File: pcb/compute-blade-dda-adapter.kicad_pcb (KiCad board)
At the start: 2 copper layers, 49 x 16 mm, 2 parts, among them J1 HLE-105-02-L-DV-PE-BE, J2 MTLW-106-06-G-D-035 REVERSE

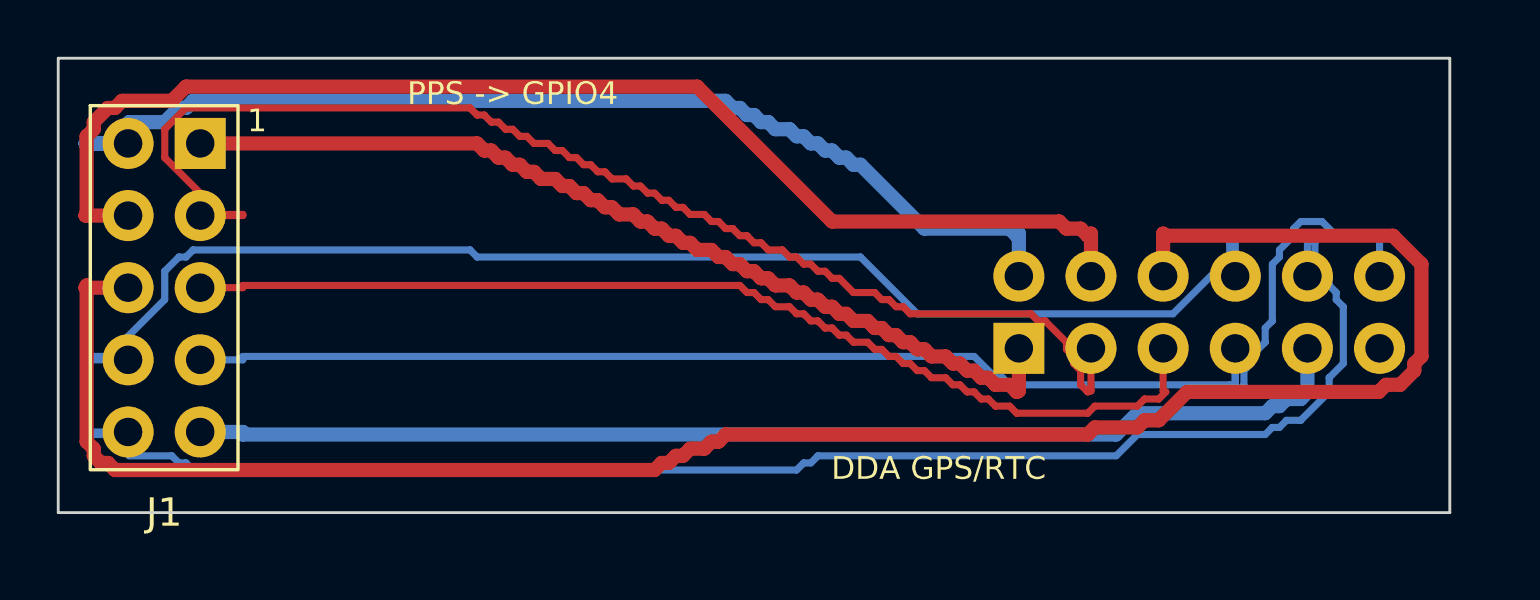
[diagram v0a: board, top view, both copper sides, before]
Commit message: Respect square pin-one pad clearances
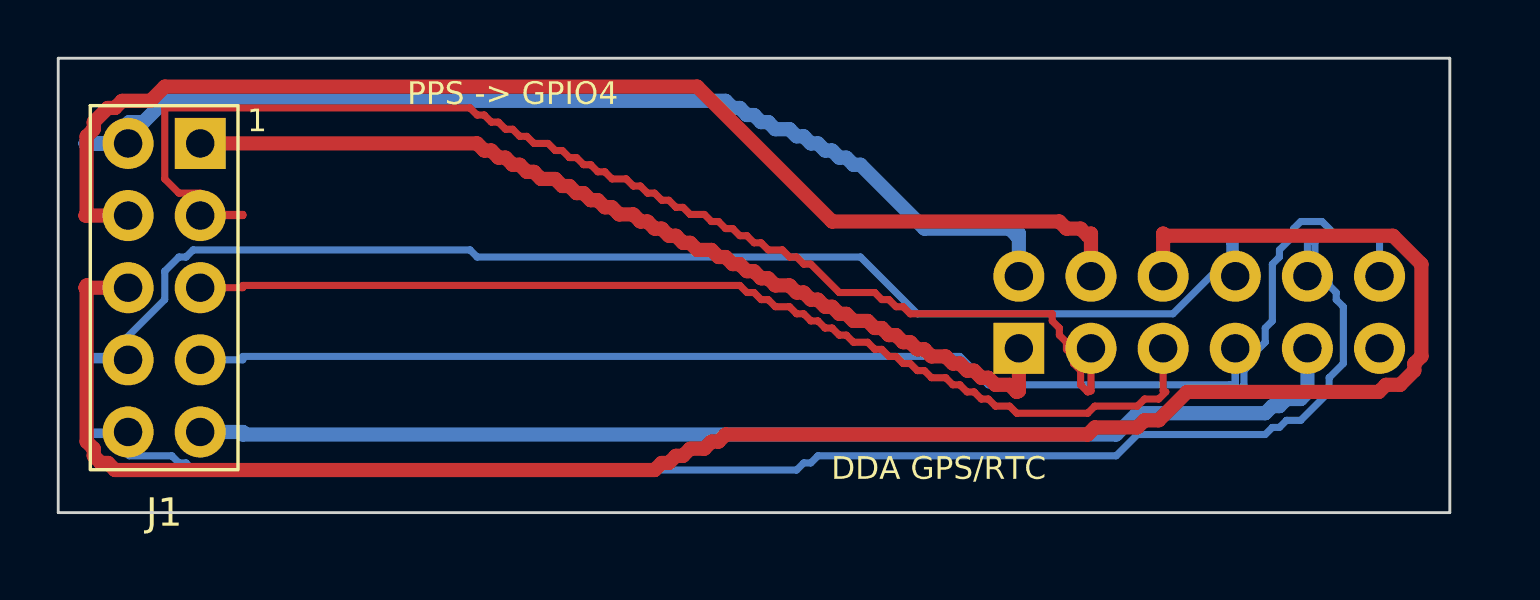
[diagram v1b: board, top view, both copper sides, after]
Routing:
- net SDA_GPIO2: track 45.3 -> 46.4 mm
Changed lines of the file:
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@@
   (segment (start 95.96 60.16) (end 96.75 60.16) (width 0.5) (layer "B.Cu") (net 2))
   (segment (start 96.75 60.16) (end 97.5 59.41) (width 0.5) (layer "B.Cu") (net 2))
-  (segment (start 97.5 59.41) (end 98.75 59.41) (width 0.5) (layer "B.Cu") (net 2))
-  (segment (start 98.75 59.41) (end 99.25 58.91) (width 0.5) (layer "B.Cu") (net 2))
-  (segment (start 99.25 58.91) (end 99.5 58.91) (width 0.5) (layer "B.Cu") (net 2))
-  (segment (start 99.5 58.91) (end 99.75 58.66) (width 0.5) (layer "B.Cu") (net 2))
-  (segment (start 99.75 58.66) (end 118.5 58.66) (width 0.5) (layer "B.Cu") (net 2))
+  (segment (start 97.5 59.41) (end 98 59.41) (width 0.5) (layer "B.Cu") (net 2))
+  (segment (start 98 59.41) (end 98.75 58.66) (width 0.5) (layer "B.Cu") (net 2))
+  (segment (start 98.75 58.66) (end 118.5 58.66) (width 0.5) (layer "B.Cu") (net 2))
   (segment (start 118.5 58.66) (end 118.75 58.91) (width 0.5) (layer "B.Cu") (net 2))
   (segment (start 118.75 58.91) (end 119 58.91) (width 0.5) (layer "B.Cu") (net 2))
@@
   (segment (start 101.5 62.7) (end 101.5 62.66) (width 0.25) (layer "F.Cu") (net 3))
   (segment (start 101.5 62.66) (end 100.75 62.66) (width 0.25) (layer "F.Cu") (net 3))
-  (segment (start 100.75 62.66) (end 98.75 60.66) (width 0.25) (layer "F.Cu") (net 3))
-  (segment (start 98.75 60.66) (end 98.75 59.66) (width 0.25) (layer "F.Cu") (net 3))
-  (segment (start 98.75 59.66) (end 99.5 58.91) (width 0.25) (layer "F.Cu") (net 3))
-  (segment (start 99.5 58.91) (end 109.5 58.91) (width 0.25) (layer "F.Cu") (net 3))
+  (segment (start 100.75 62.66) (end 100 61.91) (width 0.25) (layer "F.Cu") (net 3))
+  (segment (start 100 61.91) (end 99.25 61.91) (width 0.25) (layer "F.Cu") (net 3))
+  (segment (start 99.25 61.91) (end 98.75 61.41) (width 0.25) (layer "F.Cu") (net 3))
+  (segment (start 98.75 61.41) (end 98.75 58.91) (width 0.25) (layer "F.Cu") (net 3))
+  (segment (start 98.75 58.91) (end 109.5 58.91) (width 0.25) (layer "F.Cu") (net 3))
   (segment (start 109.5 58.91) (end 109.75 59.16) (width 0.25) (layer "F.Cu") (net 3))
   (segment (start 109.75 59.16) (end 110 59.16) (width 0.25) (layer "F.Cu") (net 3))
@@
   (segment (start 121 64.16) (end 121.25 64.41) (width 0.25) (layer "F.Cu") (net 3))
   (segment (start 121.25 64.41) (end 121.5 64.41) (width 0.25) (layer "F.Cu") (net 3))
-  (segment (start 121.5 64.41) (end 121.75 64.66) (width 0.25) (layer "F.Cu") (net 3))
-  (segment (start 121.75 64.66) (end 122 64.66) (width 0.25) (layer "F.Cu") (net 3))
-  (segment (start 122 64.66) (end 122.25 64.91) (width 0.25) (layer "F.Cu") (net 3))
-  (segment (start 122.25 64.91) (end 122.5 64.91) (width 0.25) (layer "F.Cu") (net 3))
-  (segment (start 122.5 64.91) (end 123 65.41) (width 0.25) (layer "F.Cu") (net 3))
-  (segment (start 123 65.41) (end 123.75 65.41) (width 0.25) (layer "F.Cu") (net 3))
+  (segment (start 121.5 64.41) (end 122.5 65.41) (width 0.25) (layer "F.Cu") (net 3))
+  (segment (start 122.5 65.41) (end 123.75 65.41) (width 0.25) (layer "F.Cu") (net 3))
   (segment (start 123.75 65.41) (end 124 65.66) (width 0.25) (layer "F.Cu") (net 3))
   (segment (start 124 65.66) (end 124.25 65.66) (width 0.25) (layer "F.Cu") (net 3))
@@
   (segment (start 124.5 65.91) (end 124.75 65.91) (width 0.25) (layer "F.Cu") (net 3))
   (segment (start 124.75 65.91) (end 125 66.16) (width 0.25) (layer "F.Cu") (net 3))
-  (segment (start 125 66.16) (end 129.25 66.16) (width 0.25) (layer "F.Cu") (net 3))
-  (segment (start 129.25 66.16) (end 129.5 66.41) (width 0.25) (layer "F.Cu") (net 3))
-  (segment (start 129.5 66.41) (end 129.75 66.41) (width 0.25) (layer "F.Cu") (net 3))
-  (segment (start 129.75 66.41) (end 130.5 67.16) (width 0.25) (layer "F.Cu") (net 3))
+  (segment (start 125 66.16) (end 130 66.16) (width 0.25) (layer "F.Cu") (net 3))
+  (segment (start 130 66.16) (end 130 66.41) (width 0.25) (layer "F.Cu") (net 3))
+  (segment (start 130 66.41) (end 130.25 66.66) (width 0.25) (layer "F.Cu") (net 3))
+  (segment (start 130.25 66.66) (end 130.25 66.91) (width 0.25) (layer "F.Cu") (net 3))
+  (segment (start 130.25 66.91) (end 130.5 67.16) (width 0.25) (layer "F.Cu") (net 3))
   (segment (start 130.5 67.16) (end 130.5 67.41) (width 0.25) (layer "F.Cu") (net 3))
   (segment (start 130.5 67.41) (end 130.75 67.66) (width 0.25) (layer "F.Cu") (net 3))
@@
   (segment (start 96.75 58.91) (end 97 58.91) (width 0.5) (layer "F.Cu") (net 4))
   (segment (start 97 58.91) (end 97.25 58.66) (width 0.5) (layer "F.Cu") (net 4))
-  (segment (start 97.25 58.66) (end 99 58.66) (width 0.5) (layer "F.Cu") (net 4))
-  (segment (start 99 58.66) (end 99.5 58.16) (width 0.5) (layer "F.Cu") (net 4))
-  (segment (start 99.5 58.16) (end 117.5 58.16) (width 0.5) (layer "F.Cu") (net 4))
+  (segment (start 97.25 58.66) (end 98.25 58.66) (width 0.5) (layer "F.Cu") (net 4))
+  (segment (start 98.25 58.66) (end 98.75 58.16) (width 0.5) (layer "F.Cu") (net 4))
+  (segment (start 98.75 58.16) (end 117.5 58.16) (width 0.5) (layer "F.Cu") (net 4))
   (segment (start 117.5 58.16) (end 122.25 62.91) (width 0.5) (layer "F.Cu") (net 4))
   (segment (start 122.25 62.91) (end 130.25 62.91) (width 0.5) (layer "F.Cu") (net 4))
@@
   (segment (start 100 67.78) (end 101.5 67.78) (width 0.25) (layer "B.Cu") (net 7))
   (segment (start 101.5 67.78) (end 101.5 67.66) (width 0.25) (layer "B.Cu") (net 7))
-  (segment (start 101.5 67.66) (end 127.25 67.66) (width 0.25) (layer "B.Cu") (net 7))
-  (segment (start 127.25 67.66) (end 128 68.41) (width 0.25) (layer "B.Cu") (net 7))
-  (segment (start 128 68.41) (end 128.25 68.41) (width 0.25) (layer "B.Cu") (net 7))
-  (segment (start 128.25 68.41) (end 128.5 68.66) (width 0.25) (layer "B.Cu") (net 7))
-  (segment (start 128.5 68.66) (end 136.25 68.66) (width 0.25) (layer "B.Cu") (net 7))
+  (segment (start 101.5 67.66) (end 126.75 67.66) (width 0.25) (layer "B.Cu") (net 7))
+  (segment (start 126.75 67.66) (end 127.75 68.66) (width 0.25) (layer "B.Cu") (net 7))
+  (segment (start 127.75 68.66) (end 136.25 68.66) (width 0.25) (layer "B.Cu") (net 7))
   (segment (start 136.25 68.66) (end 136.5 68.91) (width 0.25) (layer "B.Cu") (net 7))
   (segment (start 136.5 68.91) (end 136.445 68.875) (width 0.25) (layer "B.Cu") (net 7))

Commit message: Use conventional J2 on 1.0 mm adapter
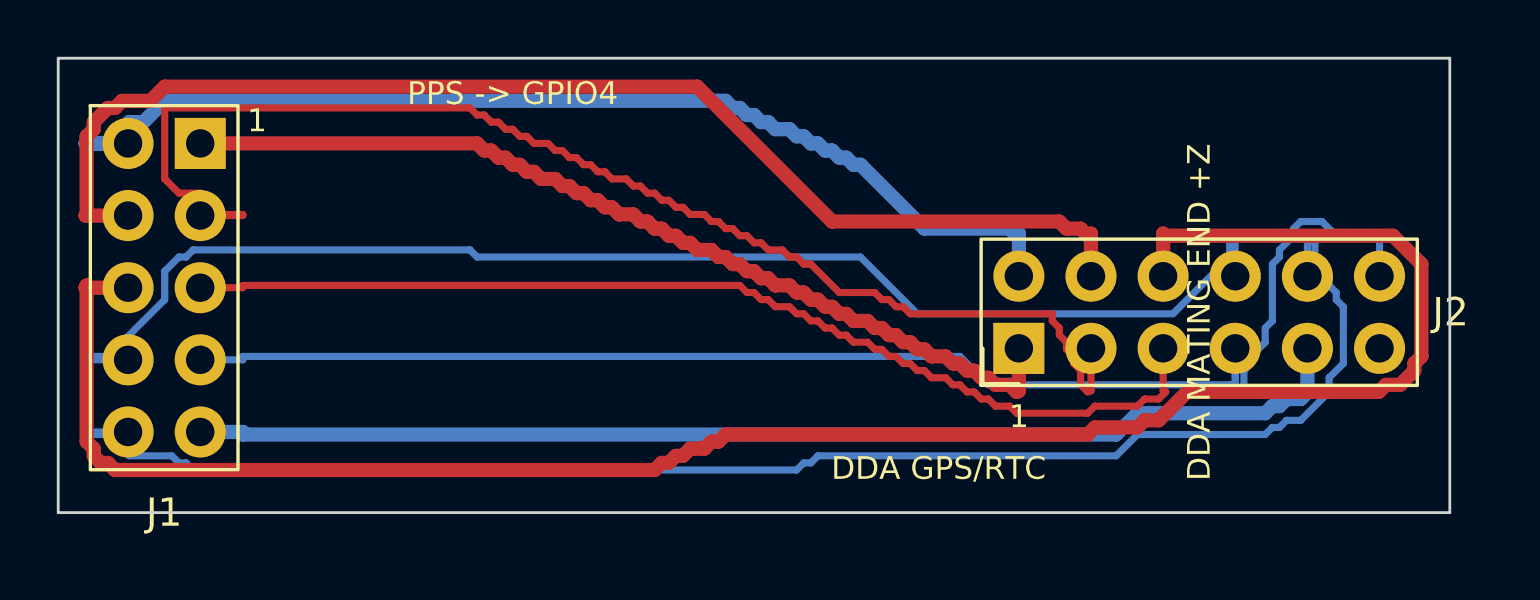
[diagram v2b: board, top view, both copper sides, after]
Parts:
- J2: value MTLW-106-06-G-D-035 REVERSE -> MTLW-106-05-G-D-140; footprint Adapter:Samtec_MTLW-106-06-G-D-035_Reverse -> Adapter:Samtec_MTLW-106-05-G-D-140; moved to F.Cu
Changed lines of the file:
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@@
 (kicad_pcb (version 20240108) (generator pcbnew)
-  (general (thickness 0.6))
+  (general (thickness 1))
   (paper "A4")
   (layers
@@
       (layer "F.SilkS" (type "Top Silk Screen")) (layer "F.Mask" (type "Top Solder Mask"))
       (layer "F.Cu" (type "copper") (thickness 0.035))
-      (layer "dielectric 1" (type "core") (thickness 0.53) (material "FR4") (epsilon_r 4.5) (loss_tangent 0.02))
+      (layer "dielectric 1" (type "core") (thickness 0.93) (material "FR4") (epsilon_r 4.5) (loss_tangent 0.02))
       (layer "B.Cu" (type "copper") (thickness 0.035))
       (layer "B.Mask" (type "Bottom Solder Mask")) (layer "B.SilkS" (type "Bottom Silk Screen"))
@@
     (model "${KIPRJMOD}/../mechanical/generated/j1_hle_105_02_l_dv_pe_be.step" (offset (xyz 0 0 0)) (scale (xyz 1 1 1)) (rotate (xyz 0 0 0)))
   )
-  (footprint "Adapter:Samtec_MTLW-106-06-G-D-035_Reverse"
-    (layer "B.Cu")
+  (footprint "Adapter:Samtec_MTLW-106-05-G-D-140"
+    (layer "F.Cu")
     (at 128.825 67.375 90)
-    (descr "Samtec MTLW-106-06-G-D-035 reverse-mounted pass-through 2x6 header")
-    (tags "Samtec MTLW reverse pass through 2x6 2.54mm")
-    (property "Reference" "J2" (at 1.27 15.2 0) (layer "B.SilkS")
- (effects (font (size 1 1) (thickness 0.15)) (justify mirror)))
-    (property "Value" "MTLW-106-06-G-D-035 REVERSE" (at 1.27 15.2 0) (layer "B.Fab")
- (effects (font (size 1 1) (thickness 0.15)) (justify mirror)))
+    (descr "Samtec MTLW-106-05-G-D-140 conventional 2x6 vertical header")
+    (tags "Samtec MTLW conventional vertical 2x6 2.54mm")
+    (property "Reference" "J2" (at 1.27 15.2 0) (layer "F.SilkS")
+ (effects (font (size 1 1) (thickness 0.15))))
+    (property "Value" "MTLW-106-05-G-D-140" (at 1.27 15.2 0) (layer "F.Fab")
+ (effects (font (size 1 1) (thickness 0.15))))
     (attr through_hole)
     (fp_rect (start -1.745 -1.77) (end 4.285 14.47)
-      (stroke (width 0.05) (type solid)) (fill none) (layer "B.CrtYd")
+      (stroke (width 0.05) (type solid)) (fill none) (layer "F.CrtYd")
 )
     (fp_rect (start -1.305 -1.33) (end 3.845 14.03)
-      (stroke (width 0.12) (type solid)) (fill none) (layer "B.SilkS")
+      (stroke (width 0.12) (type solid)) (fill none) (layer "F.SilkS")
 )
     (fp_rect (start -1.245 -1.27) (end 3.785 13.97)
-      (stroke (width 0.1) (type solid)) (fill none) (layer "B.Fab")
+      (stroke (width 0.1) (type solid)) (fill none) (layer "F.Fab")
 )
     (fp_line (start -1.245 -1.27) (end 0 -1.27)
-      (stroke (width 0.12) (type solid)) (layer "B.SilkS")
+      (stroke (width 0.12) (type solid)) (layer "F.SilkS")
 )
     (fp_line (start -1.245 -1.27) (end -1.245 0)
-      (stroke (width 0.12) (type solid)) (layer "B.SilkS")
+      (stroke (width 0.12) (type solid)) (layer "F.SilkS")
 )
-    (fp_text user "1" (at -2.4 0 0) (layer "B.SilkS")
- (effects (font (size 0.8 0.8) (thickness 0.14)) (justify mirror)))
-    (fp_text user "REVERSE / DDA ABOVE" (at 1.27 6.35 90) (layer "B.SilkS")
- (effects (font (size 0.65 0.65) (thickness 0.11)) (justify mirror)))
+    (fp_text user "1" (at -2.4 0 0) (layer "F.SilkS")
+ (effects (font (size 0.8 0.8) (thickness 0.14))))
+    (fp_text user "DDA MATING END +Z" (at 1.27 6.35 90) (layer "F.SilkS")
+ (effects (font (size 0.8 0.8) (thickness 0.12))))
     (pad "1" thru_hole rect (at 0 0)
       (size 1.8 1.8) (drill 1) (layers "*.Cu" "*.Mask") (net 1 "3V3")
@@
       (size 1.8 1.8) (drill 1) (layers "*.Cu" "*.Mask") (net 7 "PPS_GPIO4")
 )
-    (model "${KIPRJMOD}/../mechanical/generated/j2_mtlw_106_06_g_d_035_reverse.step" (offset (xyz 0 0 0)) (scale (xyz 1 1 1)) (rotate (xyz 0 0 0)))
+    (model "${KIPRJMOD}/../mechanical/generated/j2_mtlw_106_05_g_d_140.step" (offset (xyz 0 0 0)) (scale (xyz 1 1 1)) (rotate (xyz 0 0 0)))
   )
   (gr_rect (start 95 57.16) (end 144 73.16)
